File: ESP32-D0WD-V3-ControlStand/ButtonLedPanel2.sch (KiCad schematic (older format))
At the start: 32 parts

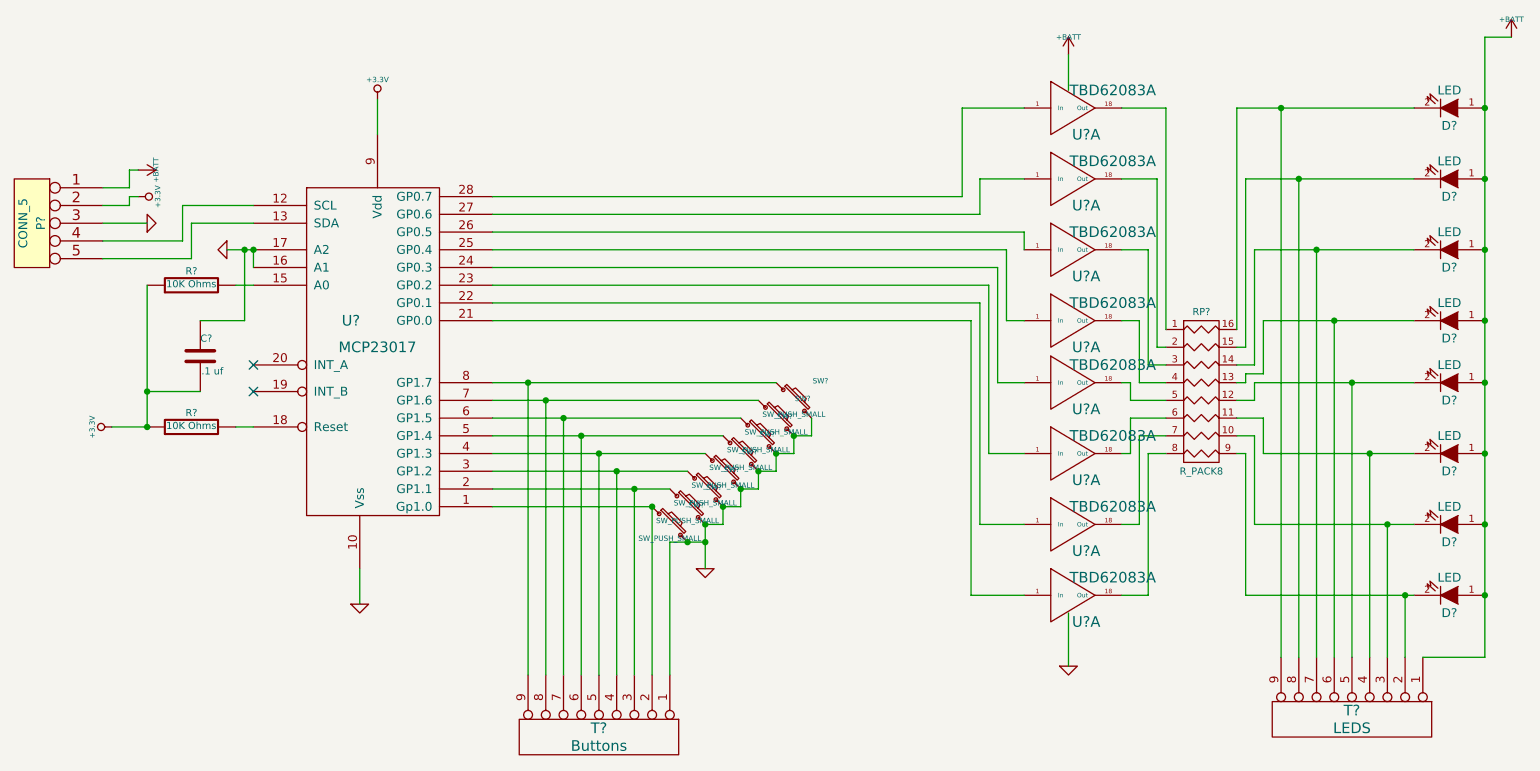
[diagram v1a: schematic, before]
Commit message: Completed parts spec for ESP32-D0WD-V3-ControlStand.
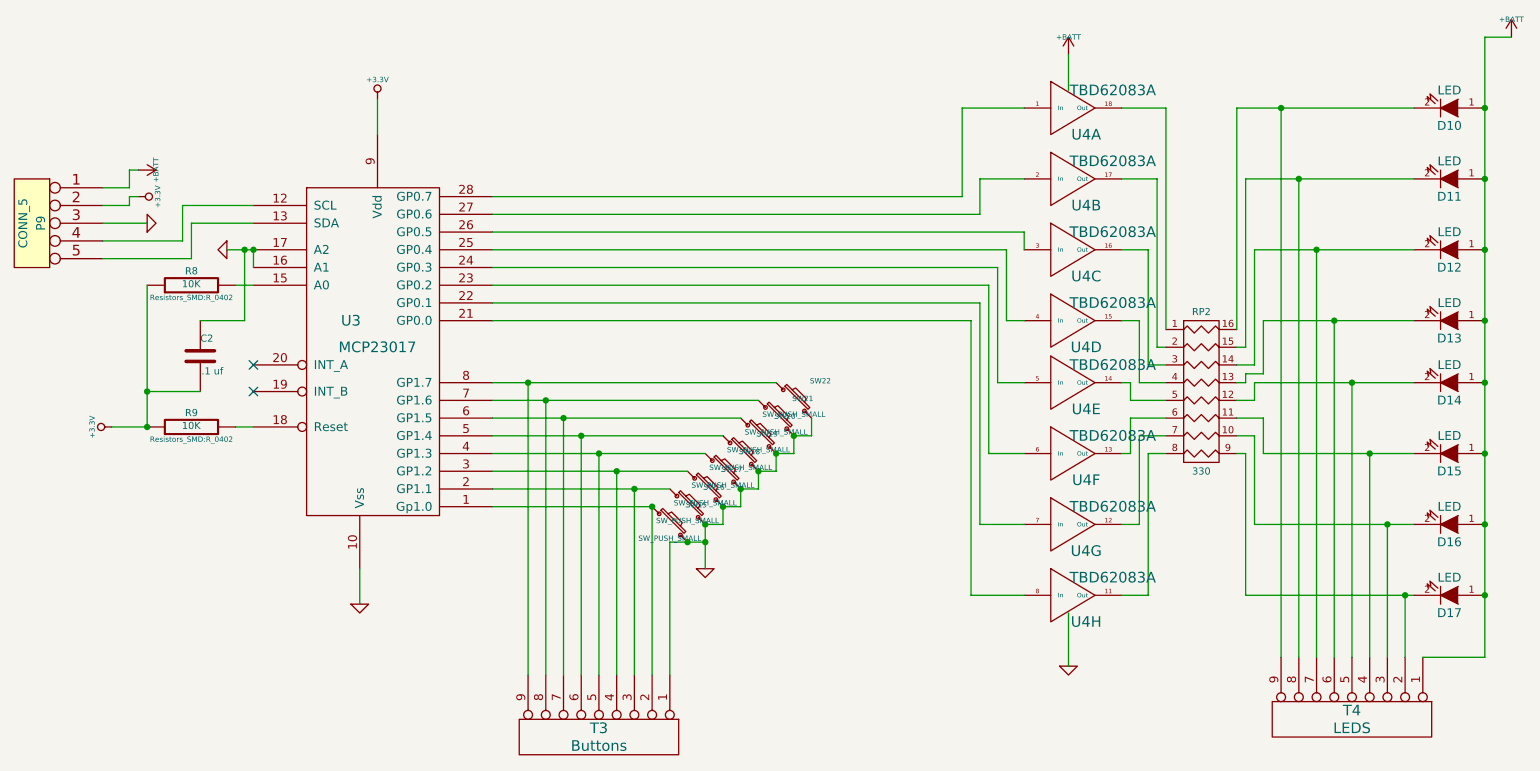
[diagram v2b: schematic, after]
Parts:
- C2: renamed from C?; footprint ~ -> Capacitors_SMD:C_0603; Mouser Part Number (none) -> 710-885012206095
- D10, D11, D12, D13, D14, D15, D16, D17: renamed from D?; footprint ~ -> LEDs:LED_D5.0mm
- P9: renamed from P?; footprint ~ -> Pin_Headers:Pin_Header_Angled_1x05_Pitch2.54mm; Mouser Part Number (none) -> 649-1012937990501BLF
- R8, R9: renamed from R?; value 10K Ohms -> 10K; footprint ~ -> Resistors_SMD:R_0402; Mouser Part Number (none) -> 603-RC0402JR-0710KL
- RP2: renamed from RP?; value R_PACK8 -> 330; footprint ~ -> 48xxP:4816P; Mouser Part Number (none) -> 652-4816P-T1LF-330
- SW15, SW16, SW17, SW18, SW19, SW20, SW21, SW22: renamed from SW?; footprint ~ -> Buttons_Switches_THT:SW_PUSH_6mm; Mouser Part Number (none) -> 179-TS026660BK160LCR
- T3, T4: renamed from T?; footprint ~ -> Connectors_Terminal_Blocks:TerminalBlock_Pheonix_MPT-2.54mm_9pol; Mouser Part Number (none) -> 651-1725724
- U3: renamed from U?; footprint ~ -> Housings_SOIC:SOIC-28W_7.5x17.9mm_Pitch1.27mm; Mouser Part Number (none) -> 79-MCP23017-E/SO
- U4: renamed from U?; footprint ~ -> Housings_SOIC:SOIC-18W_7.5x11.6mm_Pitch1.27mm; Mouser Part Number (none) -> 757-TBD62083AFG
- gave numbers to parts that had none: 1
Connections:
- net at U3.21 (GP0.0): now also U4.8 (In); no longer U4.1 (In)
- net at U3.22 (GP0.1): now also U4.7 (In); no longer U4.1 (In)
- net at U3.23 (GP0.2): now also U4.6 (In); no longer U4.1 (In)
- net at U3.24 (GP0.3): now also U4.5 (In); no longer U4.1 (In)
- net at U3.25 (GP0.4): now also U4.4 (In); no longer U4.1 (In)
- net at U3.26 (GP0.5): now also U4.3 (In); no longer U4.1 (In)
- net at U3.27 (GP0.6): now also U4.2 (In); no longer U4.1 (In)
- net at RP2.2 (P2): now also U4.17 (Out); no longer U4.18 (Out)
- net at RP2.3 (P3): now also U4.16 (Out); no longer U4.18 (Out)
- net at RP2.4 (P4): now also U4.15 (Out); no longer U4.18 (Out)
- net at RP2.5 (P5): now also U4.14 (Out); no longer U4.18 (Out)
- net at RP2.6 (P6): now also U4.13 (Out); no longer U4.18 (Out)
- net at RP2.7 (P7): now also U4.12 (Out); no longer U4.18 (Out)
- net at RP2.8 (P8): now also U4.11 (Out); no longer U4.18 (Out)
